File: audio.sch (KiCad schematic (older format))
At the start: 14 parts, among them J12 Audio-Jack-3, U6 PCM5141

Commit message: Almost all components placed... Saving before mirroring everything
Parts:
- added C25: 10uF 50V, Capacitors_SMD:C_1206, symbol C_Small
- added J13: Conn_01x05, symbol Conn_01x05
- added J14: Conn_01x10, symbol Conn_01x10
- added J15: Conn_01x07, symbol Conn_01x07
- added J9: Conn_01x05, Socket_Strips:Socket_Strip_Straight_1x05_Pitch2.54mm, symbol Conn_01x05
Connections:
- net GND: now also C25.2, J13.2 (Pin_2), J14.6 (Pin_6), J15.4 (Pin_4), J9.2 (Pin_2), J9.4 (Pin_4)
- net AUDIO_L: now reaches C20.1, J12.1, R13.1
- net AUDIO_L: now also J13.3 (Pin_3), J9.3 (Pin_3)
- net AUDIO_R: now reaches C19.1, J12.2, R14.1
- net AUDIO_R: now also J13.5 (Pin_5), J9.5 (Pin_5)
- new net +VSW: C25.1, J9.1 (Pin_1)
- new net AGND: J14.8 (Pin_8)
- new net AUDIO_GND: J13.4 (Pin_4)
- new net CS: J14.10 (Pin_10), J15.7 (Pin_7)
- new net IN+: J15.5 (Pin_5)
- new net IN-: J15.6 (Pin_6)
- new net INL: J14.7 (Pin_7)
- new net INR: J14.9 (Pin_9)
- new net SP+: J15.2 (Pin_2)
- new net SP-: J15.1 (Pin_1)
- new net SPL+: J14.4 (Pin_4)
- new net SPL-: J14.3 (Pin_3)
- new net SPR+: J14.2 (Pin_2)
- new net SPR-: J14.1 (Pin_1)
- new net VCC: J13.1 (Pin_1), J14.5 (Pin_5), J15.3 (Pin_3)
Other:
- note added: "OEP30W"
- note added: "OEP30Wx2"
- note added: "PCB"
- note added: "Power amp module connector"
- moved on the sheet: J12

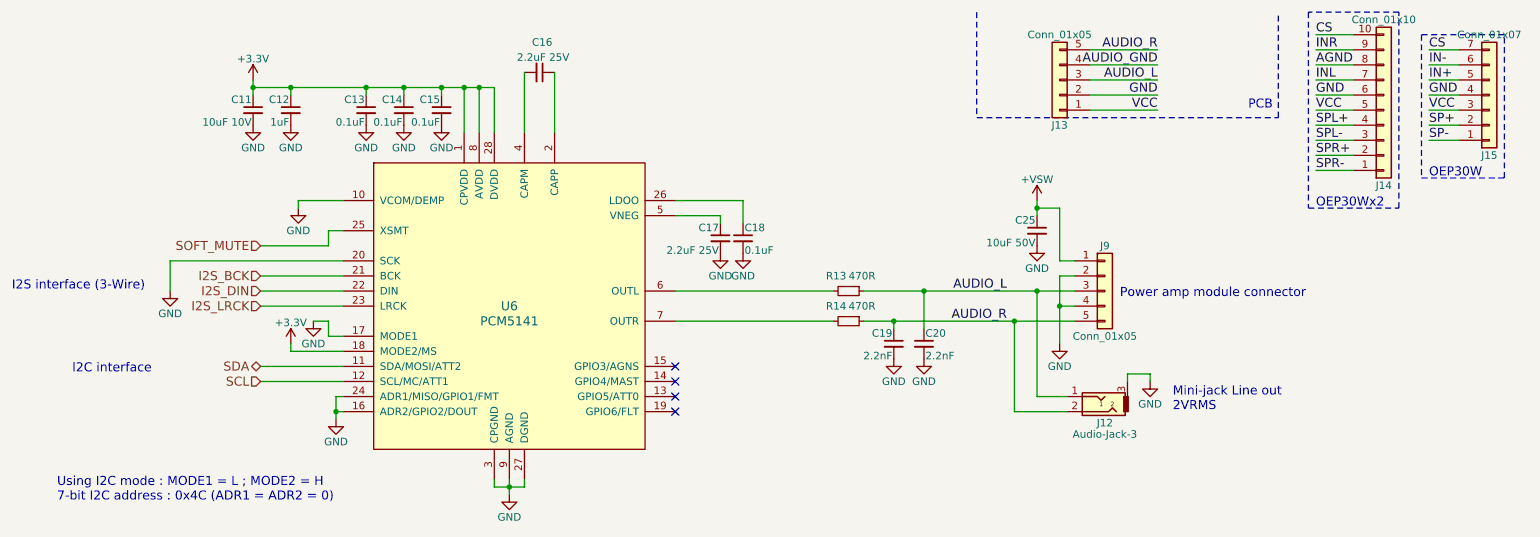
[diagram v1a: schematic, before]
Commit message: v1.0   Add 3D files with Hammond enclosures  fabrication outputs
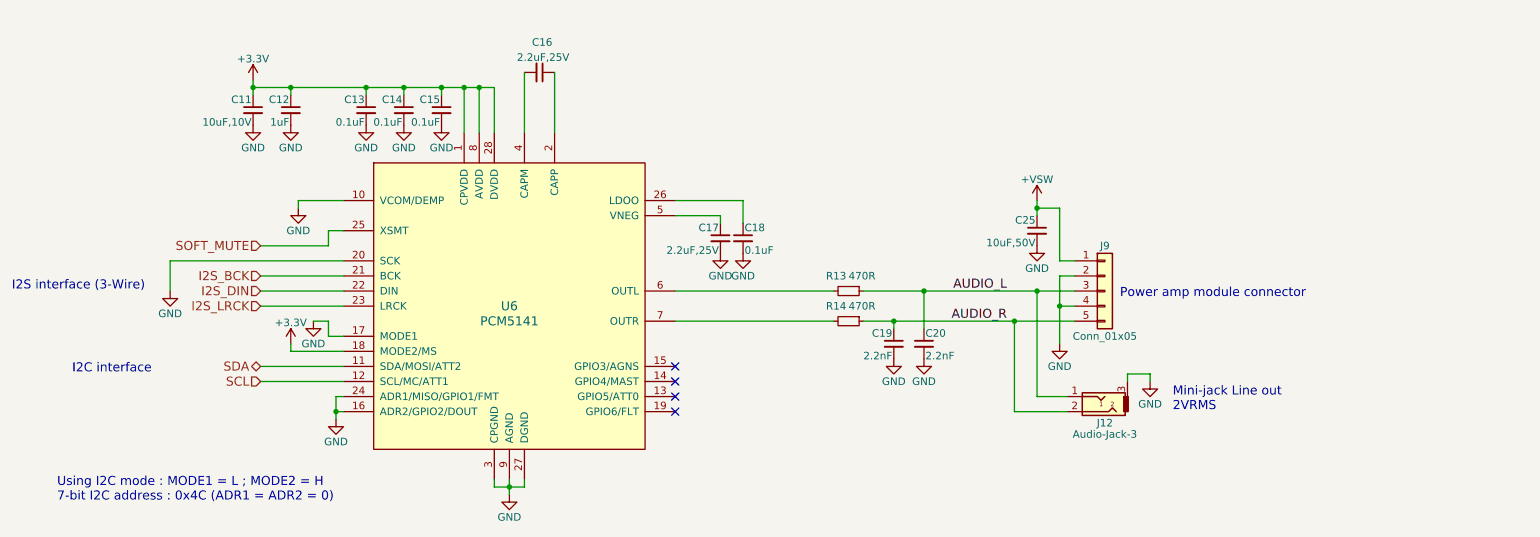
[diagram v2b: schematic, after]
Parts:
- removed J13: Conn_01x05, symbol Conn_01x05
- removed J14: Conn_01x10, symbol Conn_01x10
- removed J15: Conn_01x07, symbol Conn_01x07
- C11: value 10uF 10V -> 10uF,10V
- C16, C17: value 2.2uF 25V -> 2.2uF,25V
- C25: value 10uF 50V -> 10uF,50V
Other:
- note removed: "OEP30W"
- note removed: "OEP30Wx2"
- note removed: "PCB"
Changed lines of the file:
@@
 $EndComp
 $Comp
-L +3.3V #PWR061
+L +3.3V #PWR064
 U 1 1 5AA04578
 P 2700 2400
-F 0 "#PWR061" H 2700 2250 50  0001 C CNN
+F 0 "#PWR064" H 2700 2250 50  0001 C CNN
 F 1 "+3.3V" H 2700 2540 50  0000 C CNN
 F 2 "" H 2700 2400 50  0001 C CNN
@@
 P 2700 2600
 F 0 "C11" H 2710 2670 50  0000 L CNN
-F 1 "10uF 10V" H 2710 2520 50  0000 L CNN
+F 1 "10uF,10V" H 2710 2520 50  0000 L CNN
 F 2 "Capacitors_SMD:C_0805" H 2700 2600 50  0001 C CNN
 F 3 "" H 2700 2600 50  0001 C CNN
@@
 $EndComp
 $Comp
-L GND #PWR062
+L GND #PWR065
 U 1 1 5AA04B51
 P 2700 2700
-F 0 "#PWR062" H 2700 2450 50  0001 C CNN
+F 0 "#PWR065" H 2700 2450 50  0001 C CNN
 F 1 "GND" H 2700 2550 50  0000 C CNN
 F 2 "" H 2700 2700 50  0001 C CNN
@@
 $EndComp
 $Comp
-L GND #PWR063
+L GND #PWR066
 U 1 1 5AA04B78
 P 2950 2700
-F 0 "#PWR063" H 2950 2450 50  0001 C CNN
+F 0 "#PWR066" H 2950 2450 50  0001 C CNN
 F 1 "GND" H 2950 2550 50  0000 C CNN
 F 2 "" H 2950 2700 50  0001 C CNN
@@
 $EndComp
 $Comp
-L GND #PWR064
+L GND #PWR067
 U 1 1 5AA04B98
 P 3450 2700
-F 0 "#PWR064" H 3450 2450 50  0001 C CNN
+F 0 "#PWR067" H 3450 2450 50  0001 C CNN
 F 1 "GND" H 3450 2550 50  0000 C CNN
 F 2 "" H 3450 2700 50  0001 C CNN
@@
 $EndComp
 $Comp
-L GND #PWR065
+L GND #PWR068
 U 1 1 5AA04BB8
 P 3700 2700
-F 0 "#PWR065" H 3700 2450 50  0001 C CNN
+F 0 "#PWR068" H 3700 2450 50  0001 C CNN
 F 1 "GND" H 3700 2550 50  0000 C CNN
 F 2 "" H 3700 2700 50  0001 C CNN
@@
 $EndComp
 $Comp
-L GND #PWR066
+L GND #PWR069
 U 1 1 5AA04BD8
 P 3950 2700
-F 0 "#PWR066" H 3950 2450 50  0001 C CNN
+F 0 "#PWR069" H 3950 2450 50  0001 C CNN
 F 1 "GND" H 3950 2550 50  0000 C CNN
 F 2 "" H 3950 2700 50  0001 C CNN
@@
 P 4600 2350
 F 0 "C16" V 4400 2300 50  0000 L CNN
-F 1 "2.2uF 25V" V 4500 2200 50  0000 L CNN
+F 1 "2.2uF,25V" V 4500 2200 50  0000 L CNN
 F 2 "Capacitors_SMD:C_0603" H 4600 2350 50  0001 C CNN
 F 3 "" H 4600 2350 50  0001 C CNN
@@
 $EndComp
 $Comp
-L GND #PWR067
+L GND #PWR070
 U 1 1 5AA0515A
 P 4400 5150
-F 0 "#PWR067" H 4400 4900 50  0001 C CNN
+F 0 "#PWR070" H 4400 4900 50  0001 C CNN
 F 1 "GND" H 4400 5000 50  0000 C CNN
 F 2 "" H 4400 5150 50  0001 C CNN
@@
 P 5800 3450
 F 0 "C17" H 5810 3520 50  0000 L CNN
-F 1 "2.2uF 25V" H 5810 3370 50  0000 L CNN
+F 1 "2.2uF,25V" H 5810 3370 50  0000 L CNN
 F 2 "Capacitors_SMD:C_0603" H 5800 3450 50  0001 C CNN
 F 3 "" H 5800 3450 50  0001 C CNN
@@
 $EndComp
 $Comp
-L GND #PWR068
+L GND #PWR071
 U 1 1 5AA05C55
 P 5800 3550
-F 0 "#PWR068" H 5800 3300 50  0001 C CNN
+F 0 "#PWR071" H 5800 3300 50  0001 C CNN
 F 1 "GND" H 5800 3400 50  0000 C CNN
 F 2 "" H 5800 3550 50  0001 C CNN
@@
 $EndComp
 $Comp
-L GND #PWR069
+L GND #PWR072
 U 1 1 5AA05C7E
 P 5950 3550
-F 0 "#PWR069" H 5950 3300 50  0001 C CNN
+F 0 "#PWR072" H 5950 3300 50  0001 C CNN
 F 1 "GND" H 5950 3400 50  0000 C CNN
 F 2 "" H 5950 3550 50  0001 C CNN
@@
 $EndComp
 $Comp
-L GND #PWR070
+L GND #PWR073
 U 1 1 5AA0645F
 P 6950 4250
-F 0 "#PWR070" H 6950 4000 50  0001 C CNN
+F 0 "#PWR073" H 6950 4000 50  0001 C CNN
 F 1 "GND" H 6950 4100 50  0000 C CNN
 F 2 "" H 6950 4250 50  0001 C CNN
@@
 $EndComp
 $Comp
-L GND #PWR071
+L GND #PWR074
 U 1 1 5AA06494
 P 7150 4250
-F 0 "#PWR071" H 7150 4000 50  0001 C CNN
+F 0 "#PWR074" H 7150 4000 50  0001 C CNN
 F 1 "GND" H 7150 4100 50  0000 C CNN
 F 2 "" H 7150 4250 50  0001 C CNN
@@
 $EndComp
 $Comp
-L GND #PWR072
+L GND #PWR075
 U 1 1 5AA06BE8
 P 8650 4400
-F 0 "#PWR072" H 8650 4150 50  0001 C CNN
+F 0 "#PWR075" H 8650 4150 50  0001 C CNN
 F 1 "GND" H 8650 4250 50  0000 C CNN
 F 2 "" H 8650 4400 50  0001 C CNN
@@
 Mini-jack Line out\n2VRMS
 $Comp
-L GND #PWR073
+L GND #PWR076
 U 1 1 5AA07C48
 P 3000 3250
-F 0 "#PWR073" H 3000 3000 50  0001 C CNN
+F 0 "#PWR076" H 3000 3000 50  0001 C CNN
 F 1 "GND" H 3000 3100 50  0000 C CNN
 F 2 "" H 3000 3250 50  0001 C CNN
@@
 NoConn ~ 5500 4600
 $Comp
-L GND #PWR074
+L GND #PWR077
 U 1 1 5AA089B3
 P 3100 4000
-F 0 "#PWR074" H 3100 3750 50  0001 C CNN
+F 0 "#PWR077" H 3100 3750 50  0001 C CNN
 F 1 "GND" H 3100 3850 50  0000 C CNN
 F 2 "" H 3100 4000 50  0001 C CNN
@@
 $EndComp
 $Comp
-L +3.3V #PWR075
+L +3.3V #PWR078
 U 1 1 5AA08AB2
 P 2950 4150
-F 0 "#PWR075" H 2950 4000 50  0001 C CNN
+F 0 "#PWR078" H 2950 4000 50  0001 C CNN
 F 1 "+3.3V" H 2950 4290 50  0000 C CNN
 F 2 "" H 2950 4150 50  0001 C CNN
@@
 I2C interface
 $Comp
-L GND #PWR076
+L GND #PWR079
 U 1 1 5AA093EE
 P 3250 4650
-F 0 "#PWR076" H 3250 4400 50  0001 C CNN
+F 0 "#PWR079" H 3250 4400 50  0001 C CNN
 F 1 "GND" H 3250 4500 50  0000 C CNN
 F 2 "" H 3250 4650 50  0001 C CNN
@@
 I2S_LRCK
 $Comp
-L GND #PWR077
+L GND #PWR080
 U 1 1 5AA2F720
 P 2150 3800
-F 0 "#PWR077" H 2150 3550 50  0001 C CNN
+F 0 "#PWR080" H 2150 3550 50  0001 C CNN
 F 1 "GND" H 2150 3650 50  0000 C CNN
 F 2 "" H 2150 3800 50  0001 C CNN
@@
 	1    0    0    -1
 $EndComp
-$Comp
-L Conn_01x05 J13
-U 1 1 5AA78826
-P 8050 2400
-F 0 "J13" H 8050 2700 50  0000 C CNN
-F 1 "Conn_01x05" H 8050 2100 50  0000 C CNN
-F 2 "" H 8050 2400 50  0001 C CNN
-F 3 "" H 8050 2400 50  0001 C CNN
-	1    8050 2400
-	-1   0    0    1
-$EndComp
-Text Label 8700 2200 2    60   ~ 0
-AUDIO_R
-Text Label 8700 2300 2    60   ~ 0
-AUDIO_GND
-Text Label 8700 2400 2    60   ~ 0
-AUDIO_L
-Text Label 8700 2500 2    60   ~ 0
-GND
-Text Label 8700 2600 2    60   ~ 0
-VCC
-$Comp
-L Conn_01x10 J14
-U 1 1 5AA7903A
-P 10200 2600
-F 0 "J14" H 10200 3100 50  0000 C CNN
-F 1 "Conn_01x10" H 10200 2000 50  0000 C CNN
-F 2 "" H 10200 2600 50  0001 C CNN
-F 3 "" H 10200 2600 50  0001 C CNN
-	1    10200 2600
-	1    0    0    1
-$EndComp
 Wire Wire Line
 	2700 2400 2700 2500
@@
 Wire Wire Line
 	2150 3600 2150 3800
-Wire Wire Line
-	8250 2200 8700 2200
-Wire Wire Line
-	8250 2300 8700 2300
-Wire Wire Line
-	8250 2400 8700 2400
-Wire Wire Line
-	8250 2500 8700 2500
-Wire Wire Line
-	8250 2600 8700 2600
-Wire Notes Line
-	9700 1950 9700 3250
-Wire Notes Line
-	9700 3250 10300 3250
-Wire Notes Line
-	10300 3250 10300 1950
-Wire Notes Line
-	10300 1950 9700 1950
-Wire Notes Line
-	10450 2100 10450 3050
-Wire Notes Line
-	10450 3050 11000 3050
-Wire Notes Line
-	11000 3050 11000 2100
-Wire Notes Line
-	11000 2100 10450 2100
-Wire Wire Line
-	10000 2100 9750 2100
-Wire Wire Line
-	10000 2200 9750 2200
-Wire Wire Line
-	10000 2300 9750 2300
-Wire Wire Line
-	10000 2400 9750 2400
-Wire Wire Line
-	10000 2500 9750 2500
-Wire Wire Line
-	10000 2600 9750 2600
-Wire Wire Line
-	10000 2700 9750 2700
-Wire Wire Line
-	10000 2800 9750 2800
-Wire Wire Line
-	10000 2900 9750 2900
-Wire Wire Line
-	10000 3000 9750 3000
-Text Label 9750 2100 0    60   ~ 0
-CS
-Text Label 9750 2200 0    60   ~ 0
-INR
-Text Label 9750 2300 0    60   ~ 0
-AGND
-Text Label 9750 2400 0    60   ~ 0
-INL
-Text Label 9750 2500 0    60   ~ 0
-GND
-Text Label 9750 2600 0    60   ~ 0
-VCC
-Text Label 9750 2700 0    60   ~ 0
-SPL+
-Text Label 9750 2800 0    60   ~ 0
-SPL-
-Text Label 9750 2900 0    60   ~ 0
-SPR+
-Text Label 9750 3000 0    60   ~ 0
-SPR-
-$Comp
-L Conn_01x07 J15
-U 1 1 5AA79818
-P 10900 2500
-F 0 "J15" H 10900 2900 50  0000 C CNN
-F 1 "Conn_01x07" H 10900 2100 50  0000 C CNN
-F 2 "" H 10900 2500 50  0001 C CNN
-F 3 "" H 10900 2500 50  0001 C CNN
-	1    10900 2500
-	1    0    0    1
-$EndComp
-Wire Wire Line
-	10700 2200 10500 2200
-Wire Wire Line
-	10700 2300 10500 2300
-Wire Wire Line
-	10700 2400 10500 2400
-Wire Wire Line
-	10700 2500 10500 2500
-Wire Wire Line
-	10700 2600 10500 2600
-Wire Wire Line
-	10700 2700 10500 2700
-Wire Wire Line
-	10700 2800 10500 2800
-Text Notes 9750 3250 0    60   ~ 0
-OEP30Wx2
-Text Notes 10500 3050 0    60   ~ 0
-OEP30W
-Text Label 10500 2200 0    60   ~ 0
-CS
-Text Label 10500 2300 0    60   ~ 0
-IN-
-Text Label 10500 2400 0    60   ~ 0
-IN+
-Text Label 10500 2500 0    60   ~ 0
-GND
-Text Label 10500 2600 0    60   ~ 0
-VCC
-Text Label 10500 2700 0    60   ~ 0
-SP+
-Text Label 10500 2800 0    60   ~ 0
-SP-
 Text Label 7700 3800 2    60   ~ 0
 AUDIO_L
 Text Label 7700 4000 2    60   ~ 0
 AUDIO_R
-Wire Notes Line
-	7500 1950 7500 2650
-Wire Notes Line
-	9500 2650 9500 1950
-Text Notes 9300 2600 0    60   ~ 0
-PCB
-Wire Notes Line
-	7500 2650 9500 2650
 $Comp
 L Conn_01x05 J9
@@
 Connection ~ 7750 4000
 $Comp
-L GND #PWR078
+L GND #PWR081
 U 1 1 5AA7A385
 P 8050 4150
-F 0 "#PWR078" H 8050 3900 50  0001 C CNN
+F 0 "#PWR081" H 8050 3900 50  0001 C CNN
 F 1 "GND" H 8050 4000 50  0000 C CNN
 F 2 "" H 8050 4150 50  0001 C CNN
@@
 Connection ~ 8050 3900
 $Comp
-L +VSW #PWR079
+L +VSW #PWR082
 U 1 1 5AA7B178
 P 7900 3200
-F 0 "#PWR079" H 7900 3050 50  0001 C CNN
+F 0 "#PWR082" H 7900 3050 50  0001 C CNN
 F 1 "+VSW" H 7900 3340 50  0000 C CNN
 F 2 "" H 7900 3200 50  0001 C CNN
@@
 P 7900 3400
 F 0 "C25" H 7910 3470 50  0000 L CNN
-F 1 "10uF 50V" H 7910 3320 50  0000 L CNN
+F 1 "10uF,50V" H 7910 3320 50  0000 L CNN
 F 2 "Capacitors_SMD:C_1206" H 7900 3400 50  0001 C CNN
 F 3 "" H 7900 3400 50  0001 C CNN
@@
 $EndComp
 $Comp
-L GND #PWR080
+L GND #PWR083
 U 1 1 5AA7C466
 P 7900 3500
-F 0 "#PWR080" H 7900 3250 50  0001 C CNN
+F 0 "#PWR083" H 7900 3250 50  0001 C CNN
 F 1 "GND" H 7900 3350 50  0000 C CNN
 F 2 "" H 7900 3500 50  0001 C CNN
